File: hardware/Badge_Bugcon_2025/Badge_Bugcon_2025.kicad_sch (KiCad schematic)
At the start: 0 parts

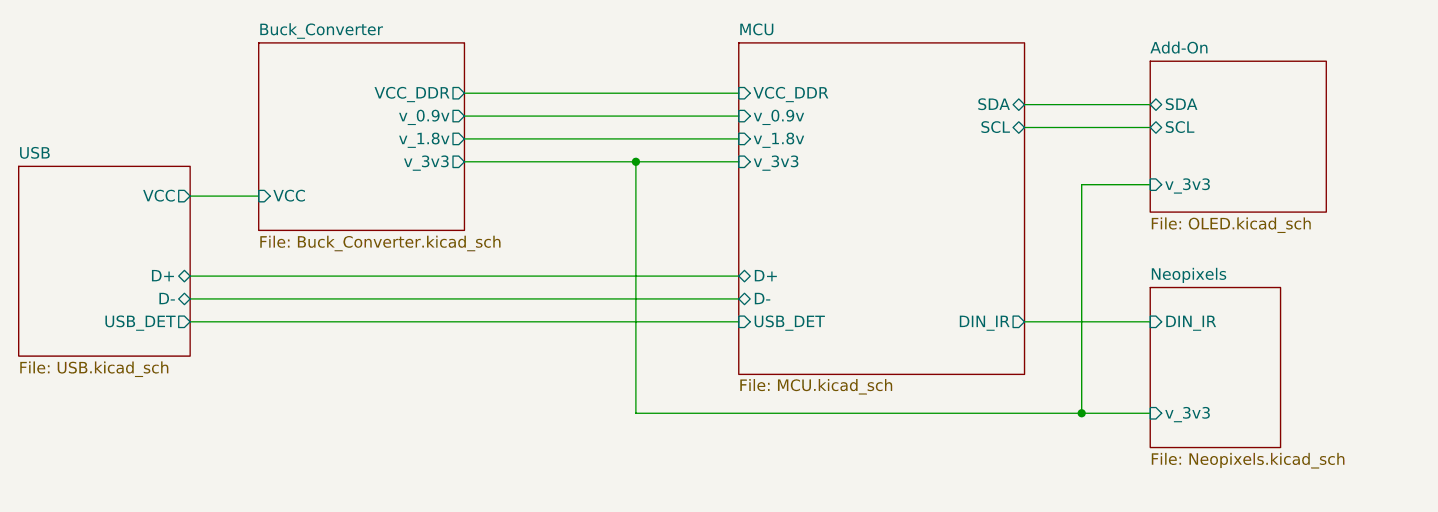
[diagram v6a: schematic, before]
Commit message: feat(Hw):Update_Schaematic_And_BOM
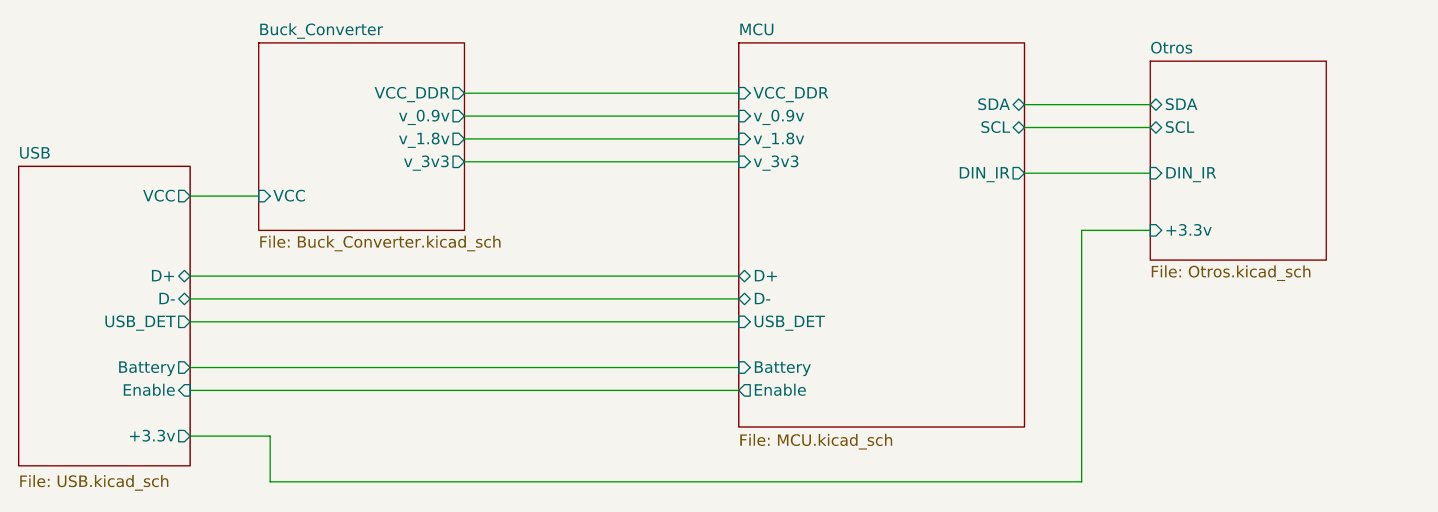
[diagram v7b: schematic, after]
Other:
- sheet Add-On renamed Otros
- removed sheet Neopixels
- sheet MCU ports: added Battery, Enable; removed none
- sheet Otros: file OLED.kicad_sch -> Otros.kicad_sch
- sheet Otros ports: added +3.3v, DIN_IR; removed v_3v3
- sheet USB ports: added +3.3v, Battery, Enable; removed none
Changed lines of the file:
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@@
 	(generator_version "9.0")
 	(paper "A4")
-	(junction
-		(at 179.07 104.14)
-		(diameter 0)
-		(color 255 23 32 1)
-	)
-	(junction
-		(at 129.54 76.2)
-		(diameter 0)
-		(color 255 23 32 1)
-	)
 	(wire
 		(pts
@@
 	(wire
 		(pts
-			(xy 110.49 76.2) (xy 129.54 76.2)
+			(xy 88.9 111.76) (xy 179.07 111.76)
 		)
 		(stroke
@@
 	(wire
 		(pts
-			(xy 129.54 76.2) (xy 129.54 104.14)
+			(xy 172.72 72.39) (xy 186.69 72.39)
+		)
+		(stroke
+			(width 0)
+			(type default)
+		)
+	)
+	(wire
+		(pts
+			(xy 80.01 93.98) (xy 140.97 93.98)
+		)
+		(stroke
+			(width 0)
+			(type default)
+		)
+	)
+	(wire
+		(pts
+			(xy 88.9 106.68) (xy 80.01 106.68)
 		)
 		(stroke
@@
 	(wire
 		(pts
-			(xy 172.72 72.39) (xy 186.69 72.39)
-		)
-		(stroke
-			(width 0)
-			(type default)
-		)
-	)
-	(wire
-		(pts
-			(xy 80.01 93.98) (xy 140.97 93.98)
+			(xy 80.01 101.6) (xy 140.97 101.6)
+		)
+		(stroke
+			(width 0)
+			(type default)
+		)
+	)
+	(wire
+		(pts
+			(xy 80.01 99.06) (xy 140.97 99.06)
+		)
+		(stroke
+			(width 0)
+			(type default)
+		)
+	)
+	(wire
+		(pts
+			(xy 179.07 83.82) (xy 179.07 111.76)
+		)
+		(stroke
+			(width 0)
+			(type default)
+			(color 255 23 32 1)
+		)
+	)
+	(wire
+		(pts
+			(xy 179.07 83.82) (xy 186.69 83.82)
+		)
+		(stroke
+			(width 0)
+			(type default)
+			(color 255 23 32 1)
+		)
+	)
+	(wire
+		(pts
+			(xy 110.49 71.12) (xy 140.97 71.12)
+		)
+		(stroke
+			(width 0)
+			(type default)
+		)
+	)
+	(wire
+		(pts
+			(xy 88.9 111.76) (xy 88.9 106.68)
+		)
+		(stroke
+			(width 0)
+			(type default)
+			(color 255 23 32 1)
+		)
+	)
+	(wire
+		(pts
+			(xy 110.49 76.2) (xy 140.97 76.2)
 		)
 		(stroke
@@
 			(width 0)
 			(type default)
-			(color 255 141 30 1)
-		)
-	)
-	(wire
-		(pts
-			(xy 179.07 78.74) (xy 179.07 104.14)
-		)
-		(stroke
-			(width 0)
-			(type default)
-			(color 255 23 32 1)
-		)
-	)
-	(wire
-		(pts
-			(xy 179.07 78.74) (xy 186.69 78.74)
-		)
-		(stroke
-			(width 0)
-			(type default)
-			(color 255 23 32 1)
-		)
-	)
-	(wire
-		(pts
-			(xy 172.72 93.98) (xy 186.69 93.98)
-		)
-		(stroke
-			(width 0)
-			(type default)
-		)
-	)
-	(wire
-		(pts
-			(xy 110.49 71.12) (xy 140.97 71.12)
-		)
-		(stroke
-			(width 0)
-			(type default)
-		)
-	)
-	(wire
-		(pts
-			(xy 129.54 76.2) (xy 140.97 76.2)
-		)
-		(stroke
-			(width 0)
-			(type default)
-			(color 255 23 32 1)
-		)
-	)
-	(wire
-		(pts
-			(xy 179.07 104.14) (xy 186.69 104.14)
-		)
-		(stroke
-			(width 0)
-			(type default)
-			(color 255 23 32 1)
 		)
 	)
@@
 	(wire
 		(pts
-			(xy 129.54 104.14) (xy 179.07 104.14)
-		)
-		(stroke
-			(width 0)
-			(type default)
-			(color 255 23 32 1)
+			(xy 172.72 77.47) (xy 186.69 77.47)
+		)
+		(stroke
+			(width 0)
+			(type default)
 		)
 	)
@@
 	(sheet
 		(at 186.69 65.024)
-		(size 19.558 16.764)
+		(size 19.558 22.098)
 		(exclude_from_sim no)
 		(in_bom yes)
@@
 			(color 0 0 0 0.0000)
 		)
-		(property "Sheetname" "Add-On"
+		(property "Sheetname" "Otros"
 			(at 186.69 64.3124 0)
 			(effects
@@
 			)
 		)
-		(property "Sheetfile" "OLED.kicad_sch"
-			(at 186.69 82.3726 0)
+		(property "Sheetfile" "Otros.kicad_sch"
+			(at 186.69 87.7066 0)
 			(effects
 				(font
@@
 			)
 		)
-		(pin "v_3v3" input
-			(at 186.69 78.74 180)
+		(pin "+3.3v" input
+			(at 186.69 83.82 180)
+			(effects
+				(font
+					(size 1.27 1.27)
+				)
+				(justify left)
+			)
+		)
+		(pin "DIN_IR" input
+			(at 186.69 77.47 180)
 			(effects
 				(font
@@
 				(path "/a95785a0-0aa1-454e-b59f-0ac64970ac71"
 					(page "7")
-				)
-			)
-		)
-	)
-	(sheet
-		(at 186.69 90.17)
-		(size 14.478 17.78)
-		(exclude_from_sim no)
-		(in_bom yes)
-		(on_board yes)
-		(dnp no)
-		(fields_autoplaced yes)
-		(stroke
-			(width 0.1524)
-			(type solid)
-		)
-		(fill
-			(color 0 0 0 0.0000)
-		)
-		(property "Sheetname" "Neopixels"
-			(at 186.69 89.4584 0)
-			(effects
-				(font
-					(size 1.27 1.27)
-				)
-				(justify left bottom)
-			)
-		)
-		(property "Sheetfile" "Neopixels.kicad_sch"
-			(at 186.69 108.5346 0)
-			(effects
-				(font
-					(size 1.27 1.27)
-				)
-				(justify left top)
-			)
-		)
-		(pin "DIN_IR" input
-			(at 186.69 93.98 180)
-			(effects
-				(font
-					(size 1.27 1.27)
-				)
-				(justify left)
-			)
-		)
-		(pin "v_3v3" input
-			(at 186.69 104.14 180)
-			(effects
-				(font
-					(size 1.27 1.27)
-				)
-				(justify left)
-			)
-		)
-		(instances
-			(project "Badge_Bugcon_2025"
-				(path "/a95785a0-0aa1-454e-b59f-0ac64970ac71"
-					(page "5")
 				)
 			)
@@
 	(sheet
 		(at 60.96 76.708)
-		(size 19.05 21.082)
+		(size 19.05 33.274)
 		(exclude_from_sim no)
 		(in_bom yes)
 		(on_board yes)
 		(dnp no)
-		(fields_autoplaced yes)
 		(stroke
 			(width 0.1524)
@@
 		)
 		(property "Sheetfile" "USB.kicad_sch"
-			(at 60.96 98.3746 0)
+			(at 60.96 110.998 0)
 			(effects
 				(font
@@
 		(pin "D-" bidirectional
 			(at 80.01 91.44 0)
+			(effects
+				(font
+					(size 1.27 1.27)
+				)
+				(justify right)
+			)
+		)
+		(pin "+3.3v" output
+			(at 80.01 106.68 0)
+			(effects
+				(font
+					(size 1.27 1.27)
+				)
+				(justify right)
+			)
+		)
+		(pin "Battery" output
+			(at 80.01 99.06 0)
+			(effects
+				(font
+					(size 1.27 1.27)
+				)
+				(justify right)
+			)
+		)
+		(pin "Enable" input
+			(at 80.01 101.6 0)
 			(effects
 				(font
@@
 	(sheet
 		(at 140.97 62.992)
-		(size 31.75 36.83)
+		(size 31.75 42.672)
 		(exclude_from_sim no)
 		(in_bom yes)
@@
 		)
 		(property "Sheetfile" "MCU.kicad_sch"
-			(at 140.97 100.33 0)
+			(at 140.97 106.426 0)
 			(effects
 				(font
@@
 		)
 		(pin "DIN_IR" output
-			(at 172.72 93.98 0)
+			(at 172.72 77.47 0)
 			(effects
 				(font
@@
 			(effects
 				(font
+					(size 1.27 1.27)
+				)
+				(justify left)
+			)
+		)
+		(pin "Battery" input
+			(at 140.97 99.06 180)
+			(effects
+				(font
+					(size 1.27 1.27)
+				)
+				(justify left)
+			)
+		)
+		(pin "Enable" output
+			(at 140.97 101.6 180)
+			(effects
+				(font

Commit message: feat(Hw):Update_Schematic_And_Route
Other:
- sheet MCU ports: added PB1, PB2; removed none
- sheet Otros ports: added PB1, PB2; removed none
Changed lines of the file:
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@@
+	(wire
+		(pts
+			(xy 172.72 85.09) (xy 186.69 85.09)
+		)
+		(stroke
+			(width 0)
+			(type default)
+		)
+	)
 	(wire
 		(pts
@@
 	(wire
 		(pts
-			(xy 179.07 83.82) (xy 179.07 111.76)
+			(xy 179.07 90.17) (xy 179.07 111.76)
 		)
 		(stroke
@@
 	(wire
 		(pts
-			(xy 179.07 83.82) (xy 186.69 83.82)
+			(xy 179.07 90.17) (xy 186.69 90.17)
 		)
 		(stroke
@@
 		(pts
 			(xy 110.49 76.2) (xy 140.97 76.2)
+		)
+		(stroke
+			(width 0)
+			(type default)
+		)
+	)
+	(wire
+		(pts
+			(xy 172.72 82.55) (xy 186.69 82.55)
 		)
 		(stroke
@@
 	(sheet
 		(at 186.69 65.024)
-		(size 19.558 22.098)
+		(size 19.558 27.94)
 		(exclude_from_sim no)
 		(in_bom yes)
@@
 		)
 		(property "Sheetfile" "Otros.kicad_sch"
-			(at 186.69 87.7066 0)
+			(at 186.69 93.5486 0)
 			(effects
 				(font
@@
 		)
 		(pin "+3.3v" input
-			(at 186.69 83.82 180)
+			(at 186.69 90.17 180)
 			(effects
 				(font
@@
 		(pin "DIN_IR" input
 			(at 186.69 77.47 180)
+			(effects
+				(font
+					(size 1.27 1.27)
+				)
+				(justify left)
+			)
+		)
+		(pin "PB1" output
+			(at 186.69 82.55 180)
+			(effects
+				(font
+					(size 1.27 1.27)
+				)
+				(justify left)
+			)
+		)
+		(pin "PB2" output
+			(at 186.69 85.09 180)
 			(effects
 				(font
@@
 			)
 		)
+		(pin "PB1" input
+			(at 172.72 82.55 0)
+			(effects
+				(font
+					(size 1.27 1.27)
+				)
+				(justify right)
+			)
+		)
+		(pin "PB2" input
+			(at 172.72 85.09 0)
+			(effects
+				(font
+					(size 1.27 1.27)
+				)
+				(justify right)
+			)
+		)
